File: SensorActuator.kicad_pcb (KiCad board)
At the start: 2 copper layers, 50 x 38 mm, 32 parts, among them IC1 STM32L051K8T6, P1 CONN_02X06, P3 CONN_02X04, P4 CONN_01X04, P5 CONN_01X02, Q1 PMosfetGen, Q2 PMosfetGen, Q4 PMosfetGen, Q5 AO3401, SW1 SW_PUSH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

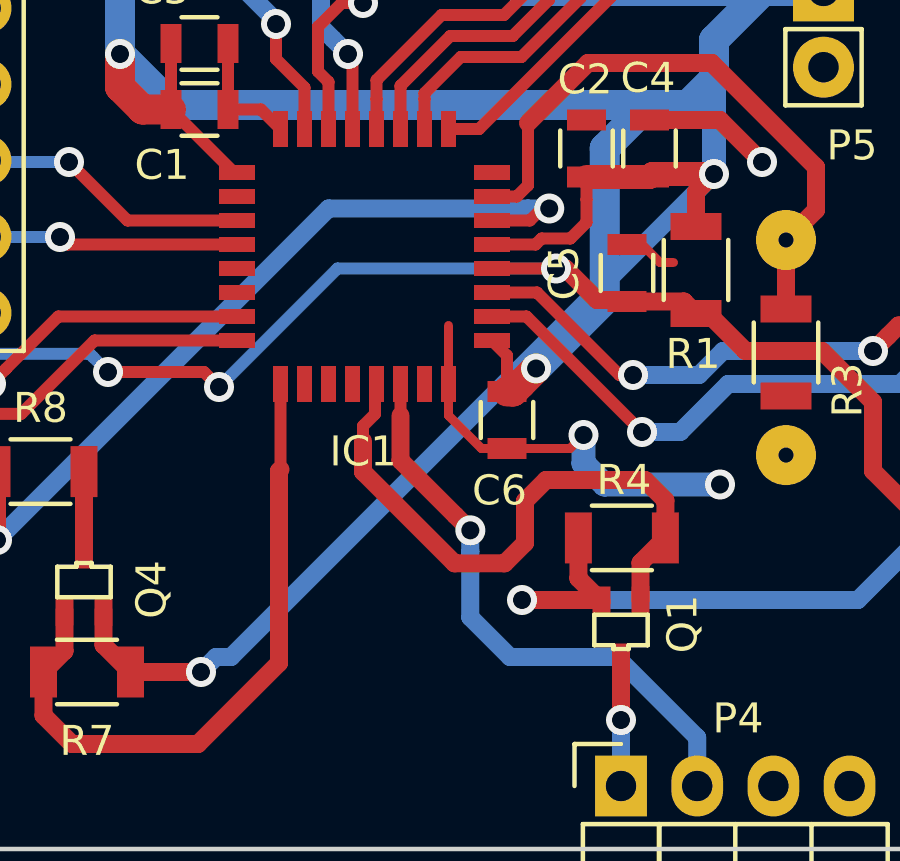
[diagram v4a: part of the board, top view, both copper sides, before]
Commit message: Fix a 5V trace
Signed-off-by: Philip Luyckx <philip.luyckx@gmail.com>
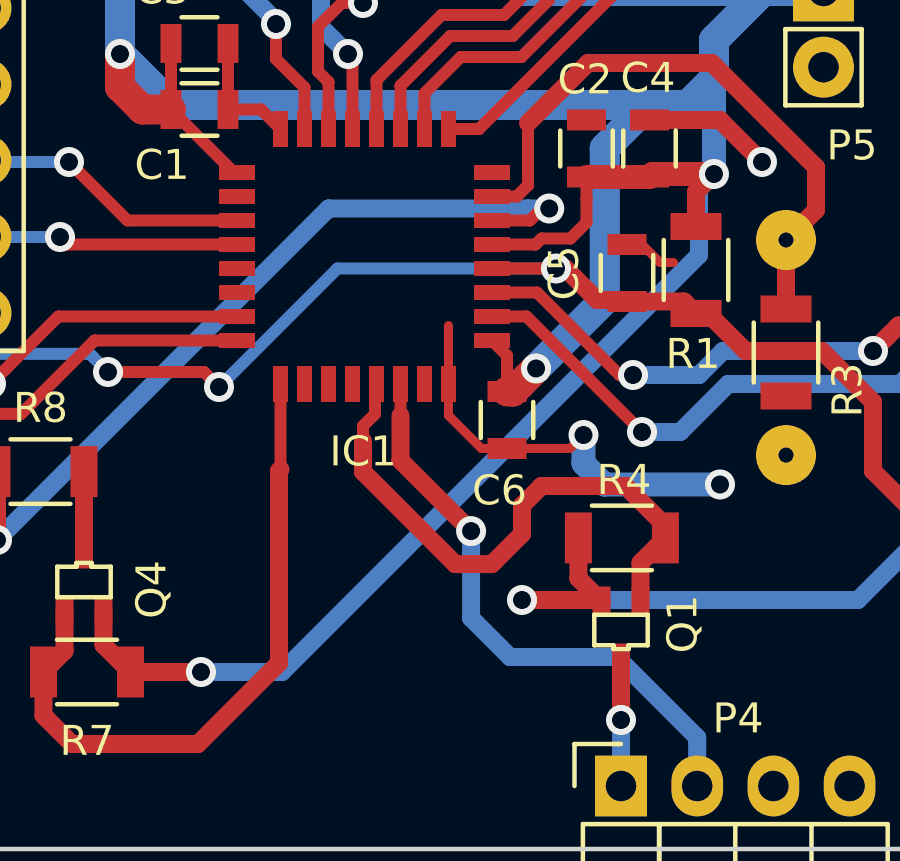
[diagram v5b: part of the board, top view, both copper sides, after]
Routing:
- net +BATT: track 132.1 -> 133.4 mm
- net DHT22_Enable: track 20.8 -> 19.9 mm
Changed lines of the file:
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@@
   )
   (setup
-    (last_trace_width 0.8)
+    (last_trace_width 0.3)
     (user_trace_width 0.3)
     (user_trace_width 0.4)
@@
     (visible_elements FFFFF77F)
     (pcbplotparams
-      (layerselection 0x00230_80000001)
+      (layerselection 0x00210_80000000)
       (usegerberextensions false)
       (excludeedgelayer false)
@@
       (outputformat 4)
       (mirror false)
-      (drillshape 2)
+      (drillshape 1)
       (scaleselection 1)
-      (outputdirectory images/pcb/))
+      (outputdirectory data/pcb/pdf))
   )
   (net 0 "")
@@
   (segment (start 101.4 73.25) (end 102.227989 73.25) (width 0.4) (layer F.Cu) (net 8))
   (segment (start 102.227989 73.25) (end 102.6 72.877989) (width 0.4) (layer F.Cu) (net 8))
+  (segment (start 100.702832 87.302832) (end 100.702832 85.109938) (width 0.6) (layer B.Cu) (net 9))
+  (segment (start 100.202833 83.902833) (end 100.702832 84.402832) (width 0.6) (layer F.Cu) (net 9))
+  (segment (start 102 88.6) (end 100.702832 87.302832) (width 0.6) (layer B.Cu) (net 9))
   (segment (start 98.35 80.55) (end 98.35 82.05) (width 0.6) (layer F.Cu) (net 9))
-  (segment (start 98.35 82.05) (end 100.177832 83.877832) (width 0.6) (layer F.Cu) (net 9))
-  (segment (start 100.677831 85.084937) (end 100.677831 84.377831) (width 0.6) (layer B.Cu) (net 9))
   (segment (start 105.556 88.6) (end 102 88.6) (width 0.6) (layer B.Cu) (net 9))
-  (segment (start 100.677831 87.277831) (end 100.677831 85.084937) (width 0.6) (layer B.Cu) (net 9))
-  (segment (start 100.177832 83.877832) (end 100.677831 84.377831) (width 0.6) (layer F.Cu) (net 9))
-  (segment (start 102 88.6) (end 100.677831 87.277831) (width 0.6) (layer B.Cu) (net 9))
   (segment (start 108.24 91.284) (end 105.556 88.6) (width 0.6) (layer B.Cu) (net 9))
-  (via (at 100.677831 84.377831) (size 1) (drill 0.6) (layers F.Cu B.Cu) (net 9))
+  (segment (start 100.702832 85.109938) (end 100.702832 84.402832) (width 0.6) (layer B.Cu) (net 9))
+  (via (at 100.702832 84.402832) (size 1) (drill 0.6) (layers F.Cu B.Cu) (net 9))
+  (segment (start 98.35 82.05) (end 100.202833 83.902833) (width 0.6) (layer F.Cu) (net 9))
   (segment (start 108.24 92.9) (end 108.24 91.284) (width 0.6) (layer B.Cu) (net 9))
   (segment (start 98.35 79.5) (end 98.35 80.55) (width 0.4) (layer F.Cu) (net 9))
   (segment (start 97.1 81.4) (end 97.1 82.428004) (width 0.6) (layer F.Cu) (net 10))
-  (segment (start 97.1 82.428004) (end 100.149829 85.477833) (width 0.6) (layer F.Cu) (net 10))
-  (segment (start 102.5 84.8) (end 102.5 83.4) (width 0.6) (layer F.Cu) (net 10))
-  (segment (start 100.149829 85.477833) (end 101.822167 85.477833) (width 0.6) (layer F.Cu) (net 10))
-  (segment (start 102.5 83.4) (end 103.2 82.7) (width 0.6) (layer F.Cu) (net 10))
-  (segment (start 101.822167 85.477833) (end 102.5 84.8) (width 0.6) (layer F.Cu) (net 10))
-  (segment (start 103.2 82.7) (end 106.5 82.7) (width 0.6) (layer F.Cu) (net 10))
-  (segment (start 106.5 82.7) (end 107.18 83.38) (width 0.6) (layer F.Cu) (net 10))
-  (segment (start 107.18 83.38) (end 107.18 84.63) (width 0.6) (layer F.Cu) (net 10))
+  (segment (start 97.1 82.428004) (end 100.17483 85.502834) (width 0.6) (layer F.Cu) (net 10))
+  (segment (start 100.17483 85.502834) (end 101.397166 85.502834) (width 0.6) (layer F.Cu) (net 10))
+  (segment (start 102.4 83.55) (end 103.05 82.9) (width 0.6) (layer F.Cu) (net 10))
+  (segment (start 101.397166 85.502834) (end 102.4 84.5) (width 0.6) (layer F.Cu) (net 10))
+  (segment (start 102.4 84.5) (end 102.4 83.55) (width 0.6) (layer F.Cu) (net 10))
+  (segment (start 103.05 82.9) (end 105.85 82.9) (width 0.6) (layer F.Cu) (net 10))
+  (segment (start 105.85 82.9) (end 107.18 84.23) (width 0.6) (layer F.Cu) (net 10))
+  (segment (start 107.18 84.23) (end 107.18 84.63) (width 0.6) (layer F.Cu) (net 10))
   (segment (start 97.55 79.5) (end 97.500001 79.549999) (width 0.4) (layer F.Cu) (net 10))
   (segment (start 97.500001 79.549999) (end 97.500001 80.500001) (width 0.4) (layer F.Cu) (net 10))
@@
   (segment (start 123.2 66.05) (end 123.2 65.118402) (width 0.3) (layer F.Cu) (net 26))
   (segment (start 87.8 85.15004) (end 87.8 82.42) (width 0.6) (layer F.Cu) (net 27))
+  (segment (start 91.7 89.1) (end 94.4 89.1) (width 0.6) (layer B.Cu) (net 28))
+  (segment (start 94.4 89.1) (end 108.300001 75.199999) (width 0.6) (layer B.Cu) (net 28))
+  (segment (start 108.300001 75.199999) (end 108.300001 72.999999) (width 0.6) (layer B.Cu) (net 28))
   (segment (start 108.300001 72.999999) (end 108.8 72.5) (width 0.6) (layer B.Cu) (net 28))
-  (segment (start 92.699999 88.600001) (end 108.300001 72.999999) (width 0.6) (layer B.Cu) (net 28))
-  (segment (start 92.199999 88.600001) (end 92.699999 88.600001) (width 0.6) (layer B.Cu) (net 28))
-  (segment (start 91.7 89.1) (end 92.199999 88.600001) (width 0.6) (layer B.Cu) (net 28))
   (segment (start 90.7 70.35) (end 89.75 70.35) (width 1) (layer F.Cu) (net 28))
   (segment (start 89.75 70.35) (end 89 69.6) (width 1) (layer F.Cu) (net 28))
